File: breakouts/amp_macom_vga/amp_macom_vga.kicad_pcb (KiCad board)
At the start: 4 copper layers, 42 x 41 mm, 52 parts, among them J101 RF_Shield_Two_Pieces, J102 CONN_01X02, J103 CONN_01X04, Q101 DMG2305UX, Q102 DMG2305UX, U101 CONN_SMA_2GND, U102 LM2776, U103 LTC2630, U104 MAAM-011100, U105 CONN_SMA_2GND, U106 LTC2054HV, U107 MAX810MTRG

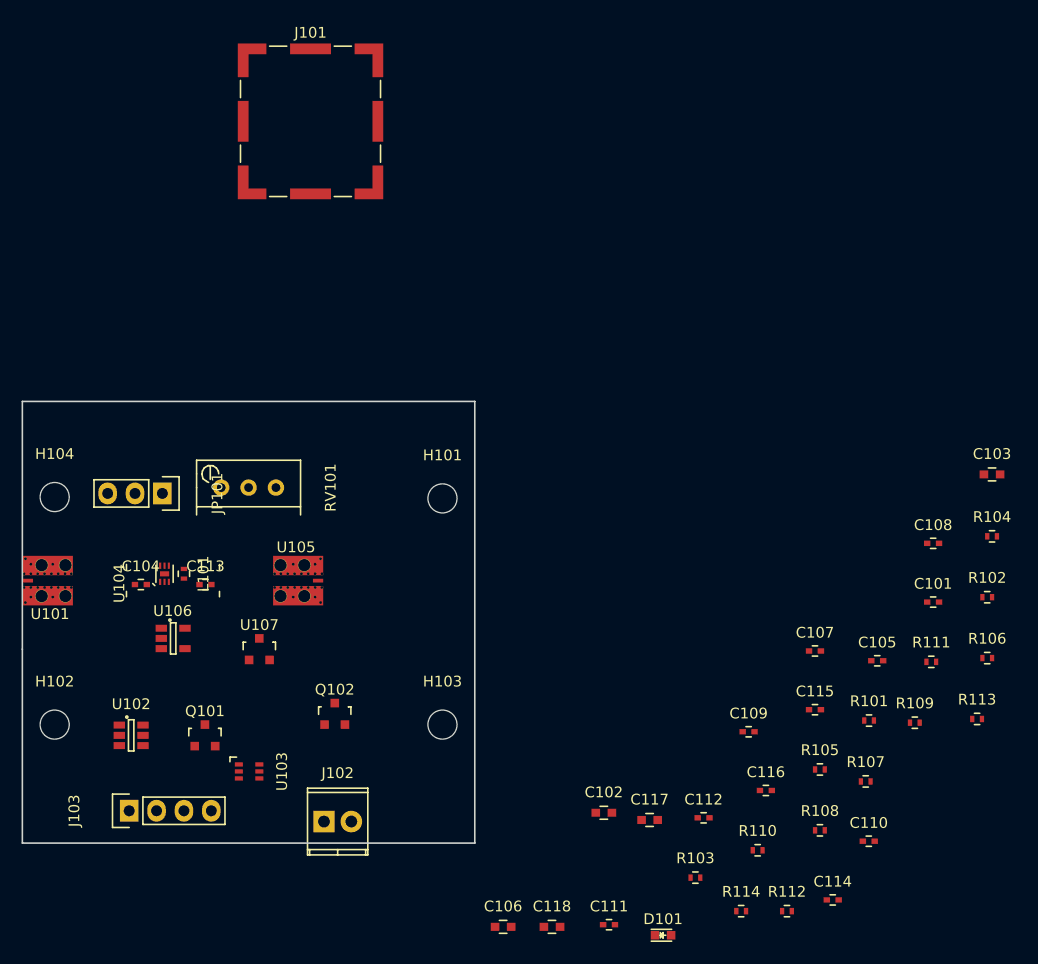
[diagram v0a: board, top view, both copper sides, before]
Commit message: finished maam-011100 board
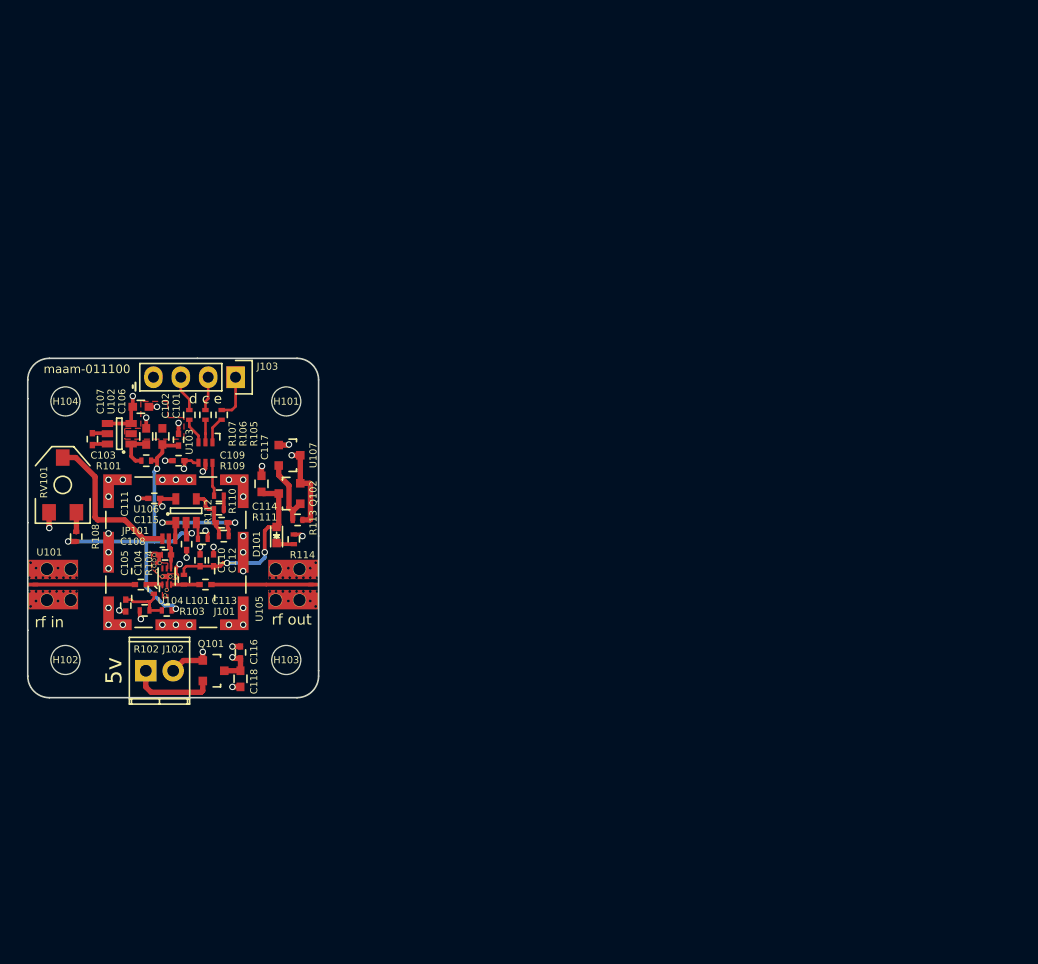
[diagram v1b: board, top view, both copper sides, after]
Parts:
- added G***: LOGO, lib:gunter, B.Cu at (166.2, 102.8)
- added REF**: VIA_OSH4LAYER_MIN, vna_footprints:VIA_OSH4LAYER_MIN, F.Cu at (163.4, 112.5)
- added REF**: VIA_OSH4LAYER_MIN, vna_footprints:VIA_OSH4LAYER_MIN, F.Cu at (163.2, 113.0)
- added REF**: VIA_OSH4LAYER_MIN, vna_footprints:VIA_OSH4LAYER_MIN, F.Cu at (162.2, 109.8)
- added REF**: VIA_OSH4LAYER_MIN, vna_footprints:VIA_OSH4LAYER_MIN, F.Cu at (162.8, 110.0)
- added REF**: VIA_OSH4LAYER_MIN, vna_footprints:VIA_OSH4LAYER_MIN, F.Cu at (162.2, 109.2)
- added REF**: VIA_OSH4LAYER_MIN, vna_footprints:VIA_OSH4LAYER_MIN, F.Cu at (162.2, 110.2)
- added REF**: VIA_OSH4LAYER_MIN, vna_footprints:VIA_OSH4LAYER_MIN, F.Cu at (162.5, 110.8)
- added REF**: VIA_OSH4LAYER_MIN, vna_footprints:VIA_OSH4LAYER_MIN, F.Cu at (163.0, 111.2)
- added REF**: VIA_OSH4LAYER_MIN, vna_footprints:VIA_OSH4LAYER_MIN, F.Cu at (164.2, 111.2)
- added REF**: VIA_OSH4LAYER_MIN, vna_footprints:VIA_OSH4LAYER_MIN, F.Cu at (163.8, 111.2)
- JP101: footprint Pin_Headers:Pin_Header_Straight_1x03 -> vna_footprints:JMP_3
- RV101: footprint Potentiometers:Potentiometer_Bourns_3296W_3-8Zoll_Inline_ScrewUp -> SMD_Packages:POT_SMD
- moved C103 78.6 mm to (161.5, 98.2), turned to 270 degrees
- moved R102 78.2 mm to (161.3, 114.4)
- moved R104 78.0 mm to (162.2, 112.4), turned to 90 degrees
- moved R106 76.0 mm to (167.0, 96.2), turned to 270 degrees
- moved R108 74.2 mm to (155.0, 107.5), turned to 270 degrees
- moved C101 71.7 mm to (164.5, 98.5), turned to 270 degrees
- moved R107 71.4 mm to (165.5, 96.2), turned to 270 degrees
- moved C108 71.3 mm to (163.2, 109.2), turned to 180 degrees
- moved R101 71.3 mm to (161.5, 100.5), turned to 180 degrees
- moved C105 69.9 mm to (159.6, 114.0), turned to 270 degrees
- moved C107 69.9 mm to (156.5, 98.5), turned to 270 degrees
- moved R109 67.9 mm to (168.2, 103.8)
- moved C110 67.3 mm to (166.5, 109.8), turned to 90 degrees
- moved R111 66.7 mm to (168.7, 107.5)
- moved C114 66.7 mm to (168.5, 106.2)
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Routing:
- net -5V: track 0.00 -> 34.2 mm, vias 0 -> 4
- net GND: track 0.00 -> 21.5 mm, vias 0 -> 44
- net +5V: track 0.00 -> 21.2 mm, vias 0 -> 5
- net /AMP_5V: track 0.00 -> 17.1 mm, vias 0 -> 2
- net Net-(JP101-Pad1): track 0.00 -> 14.5 mm
- net /AMP_VC: track 0.00 -> 11.5 mm, vias 0 -> 2
- net Net-(C113-Pad2): track 0.00 -> 9.45 mm
- net Net-(C104-Pad1): track 0.00 -> 9.45 mm
- net Net-(J102-Pad1): track 0.00 -> 7.96 mm
- net Net-(Q102-Pad1): track 0.00 -> 6.58 mm
- net Net-(C105-Pad1): track 0.00 -> 5.41 mm
- net Net-(C114-Pad1): track 0.00 -> 5.18 mm
- net /DAC_CS: track 0.00 -> 4.14 mm
- net Net-(C103-Pad2): track 0.00 -> 3.69 mm
- net /DAC_SDI: track 0.00 -> 3.38 mm
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- added copper zone on In2.Cu, net +5V
- added copper zone on F.Cu, net GND
- added copper zone on In1.Cu, net GND
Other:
- board size 42 x 41 mm -> 27 x 31.5 mm
- net class Default: clearance 0.2 -> 0.128
- rule pad_to_mask_clearance: 0.2 -> 0.05
- rule trace_clearance: 0.2 -> 0.128
- board text added: "5v"
- board text added: "d c e"
- board text added: "maam-011100"
- board text added: "rf in"
- board text added: "rf out"
